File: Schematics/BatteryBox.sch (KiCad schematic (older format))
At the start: 0 parts

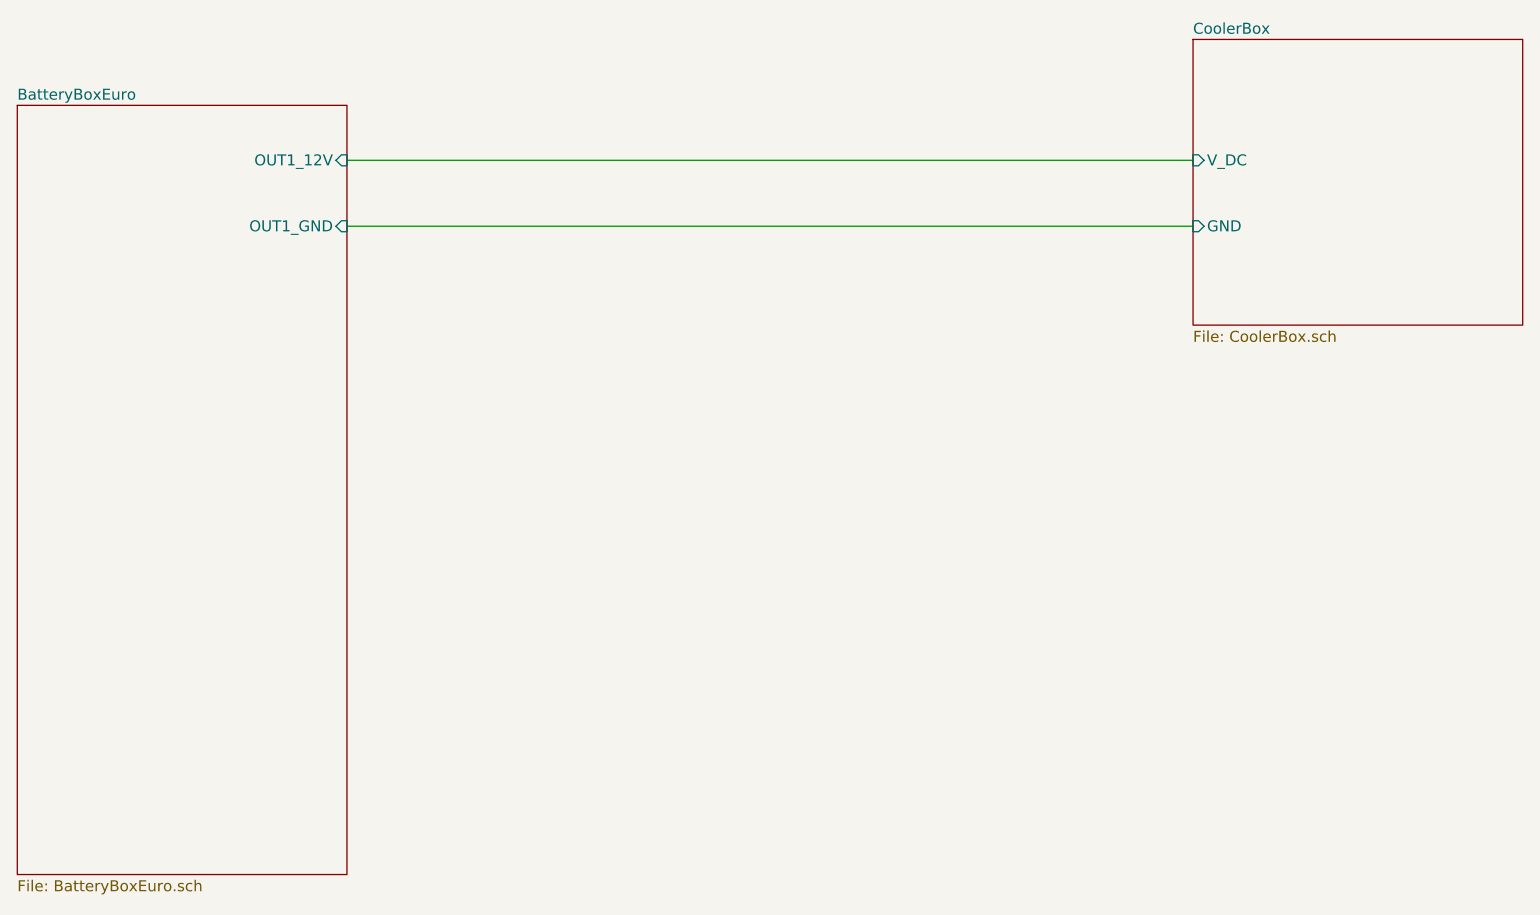
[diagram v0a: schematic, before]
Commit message: add usb charger
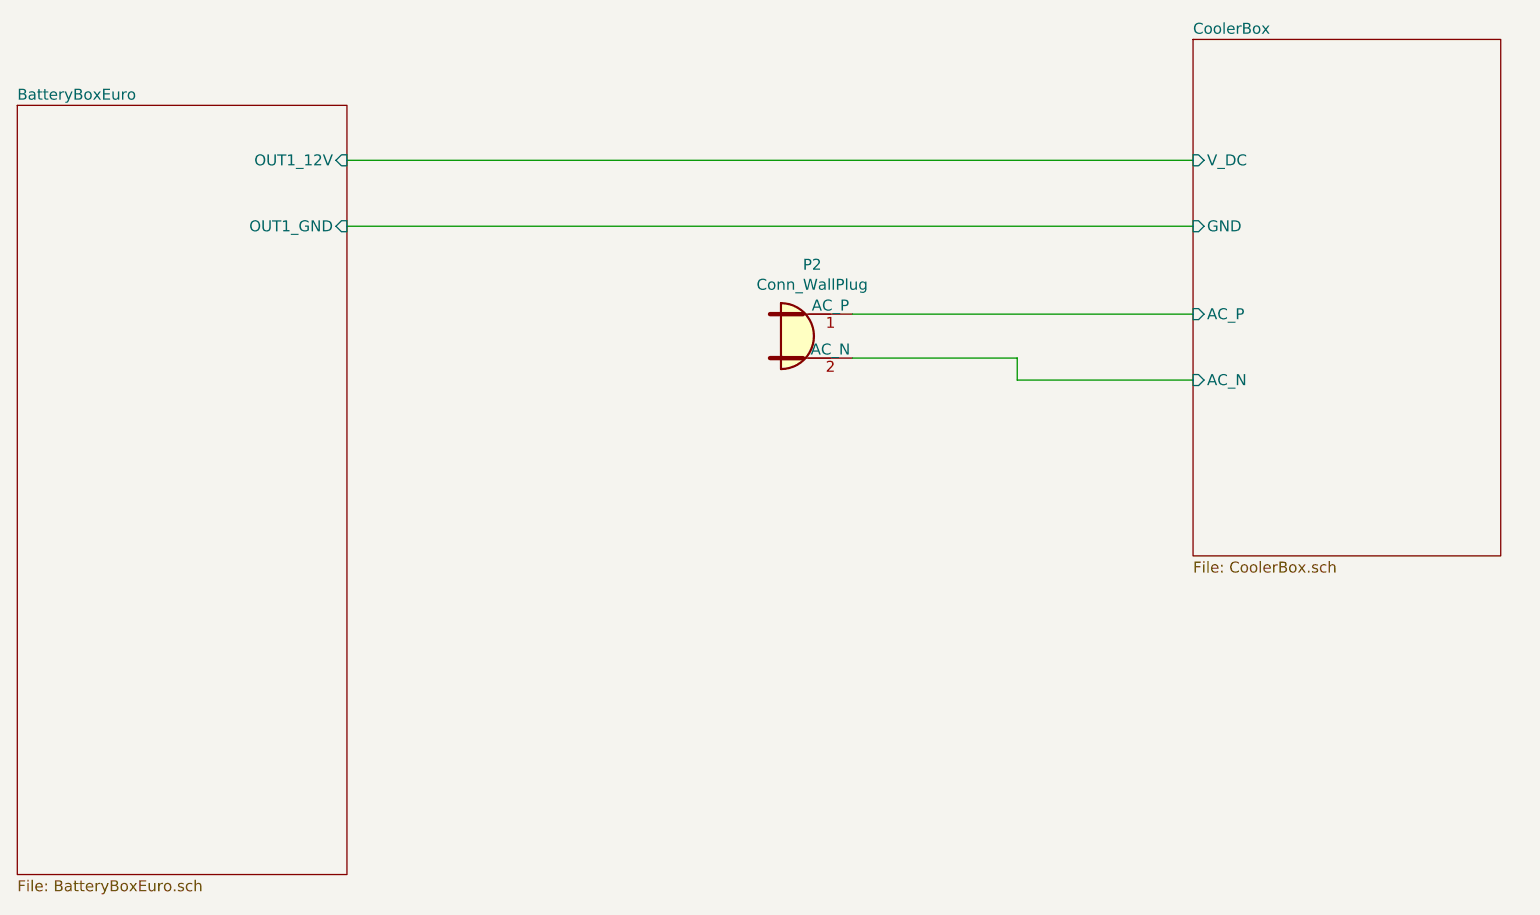
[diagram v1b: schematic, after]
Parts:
- added P2: Conn_WallPlug, symbol Connector:Conn_WallPlug
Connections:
- new net CoolerBox/AC_N: P2.2 (AC_N)
- new net CoolerBox/AC_P: P2.1 (AC_P)
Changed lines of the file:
@@
 $EndDescr
 $Sheet
-S 8350 1450 1500 1300
+S 8350 1450 1400 2350
 U 5EF099A0
 F0 "CoolerBox" 50
@@
 F2 "V_DC" I L 8350 2000 50
 F3 "GND" I L 8350 2300 50
+F4 "AC_P" I L 8350 2700 50
+F5 "AC_N" I L 8350 3000 50
 $EndSheet
 $Sheet
@@
 Wire Wire Line
 	4500 2300 8350 2300
+$Comp
+L Connector:Conn_WallPlug P2
+U 1 1 5EF0BCF3
+P 6600 2800
+F 0 "P2" H 6617 3125 50  0000 C CNN
+F 1 "Conn_WallPlug" H 6617 3034 50  0000 C CNN
+F 2 "" H 7000 2800 50  0001 C CNN
+F 3 "~" H 7000 2800 50  0001 C CNN
+	1    6600 2800
+	1    0    0    -1
+$EndComp
+Wire Wire Line
+	6800 2700 8350 2700
+Wire Wire Line
+	6800 2900 7550 2900
+Wire Wire Line
+	7550 2900 7550 3000
+Wire Wire Line
+	7550 3000 8350 3000
 $EndSCHEMATC

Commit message: add filed
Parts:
- removed P2: Conn_WallPlug, symbol Connector:Conn_WallPlug
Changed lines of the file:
@@
 $EndDescr
 $Sheet
-S 8350 1450 1400 2350
+S 8350 1450 1500 1300
 U 5EF099A0
 F0 "CoolerBox" 50
@@
 F2 "V_DC" I L 8350 2000 50
 F3 "GND" I L 8350 2300 50
-F4 "AC_P" I L 8350 2700 50
-F5 "AC_N" I L 8350 3000 50
 $EndSheet
 $Sheet
@@
 $EndSheet
 Wire Wire Line
+	4500 2300 6450 2300
+Wire Wire Line
 	4500 2000 8350 2000
 Wire Wire Line
-	4500 2300 8350 2300
-$Comp
-L Connector:Conn_WallPlug P2
-U 1 1 5EF0BCF3
-P 6600 2800
-F 0 "P2" H 6617 3125 50  0000 C CNN
-F 1 "Conn_WallPlug" H 6617 3034 50  0000 C CNN
-F 2 "" H 7000 2800 50  0001 C CNN
-F 3 "~" H 7000 2800 50  0001 C CNN
-	1    6600 2800
-	1    0    0    -1
-$EndComp
-Wire Wire Line
-	6800 2700 8350 2700
-Wire Wire Line
-	6800 2900 7550 2900
-Wire Wire Line
-	7550 2900 7550 3000
-Wire Wire Line
-	7550 3000 8350 3000
+	6450 2300 8350 2300
 $EndSCHEMATC

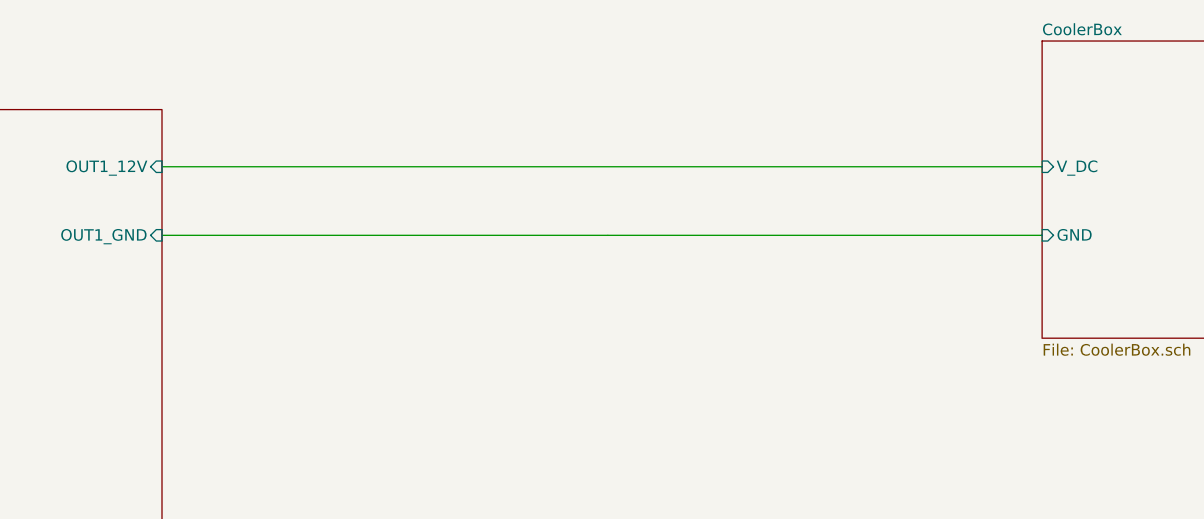
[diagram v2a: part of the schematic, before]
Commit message: add 230V
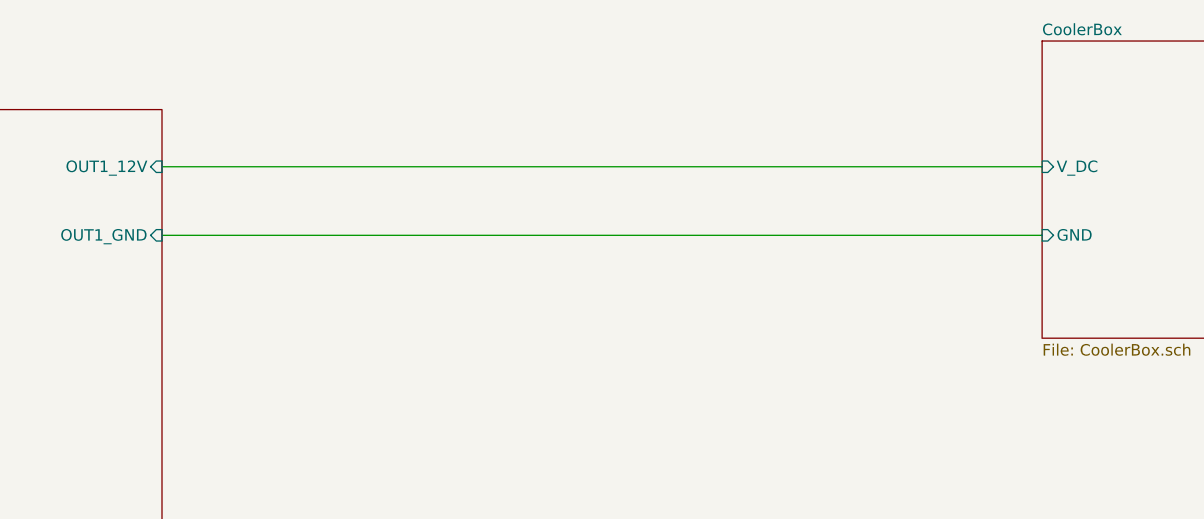
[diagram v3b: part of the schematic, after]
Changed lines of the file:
@@
 $EndSheet
-Wire Wire Line
-	4500 2300 6450 2300
 Wire Wire Line
 	4500 2000 8350 2000
 Wire Wire Line
-	6450 2300 8350 2300
+	4500 2300 8350 2300
 $EndSCHEMATC
